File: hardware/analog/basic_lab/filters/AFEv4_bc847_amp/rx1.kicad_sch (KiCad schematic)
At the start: 7 parts, among them J7 Connector_Generic_Conn_01x02, J8 Connector_Generic_Conn_01x02

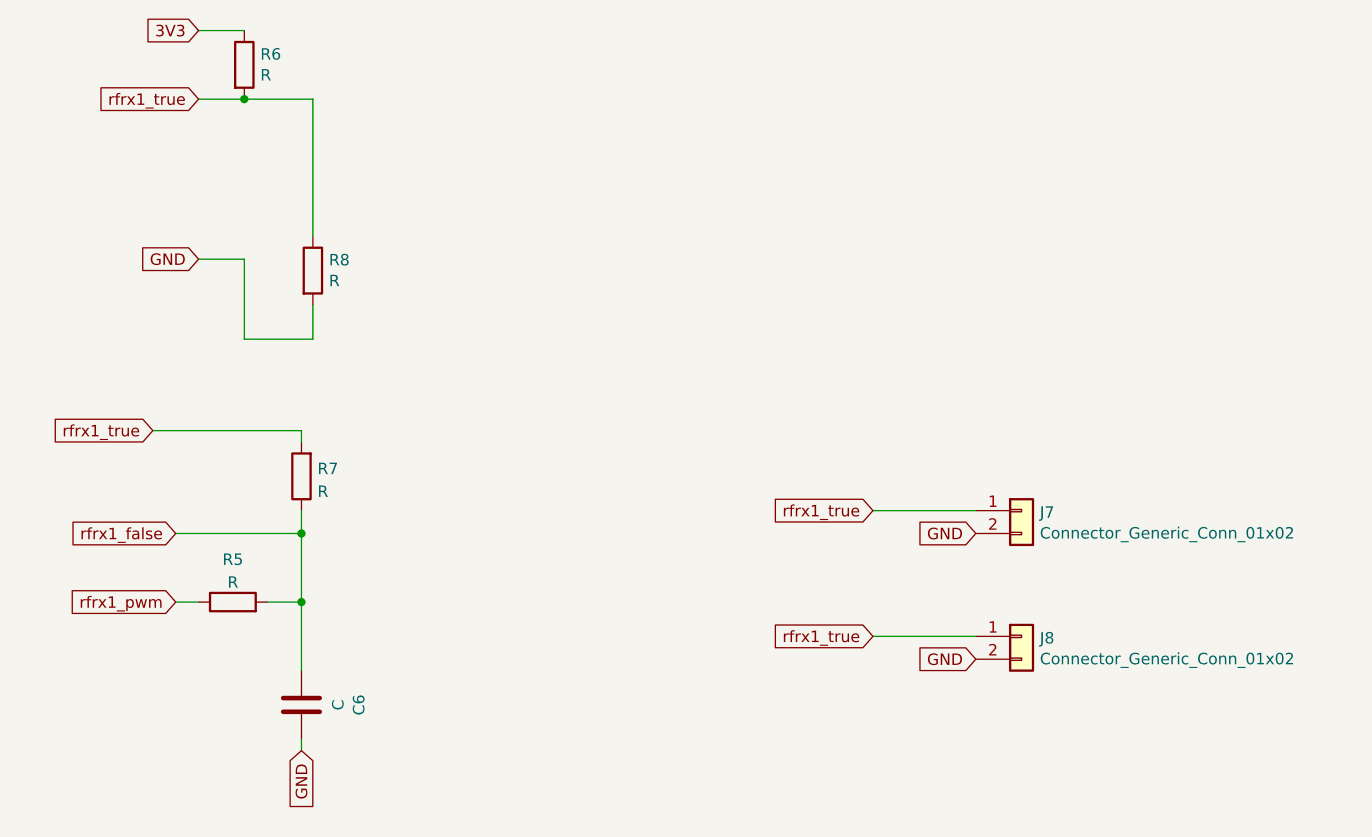
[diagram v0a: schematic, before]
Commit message: started PCB LC LPF
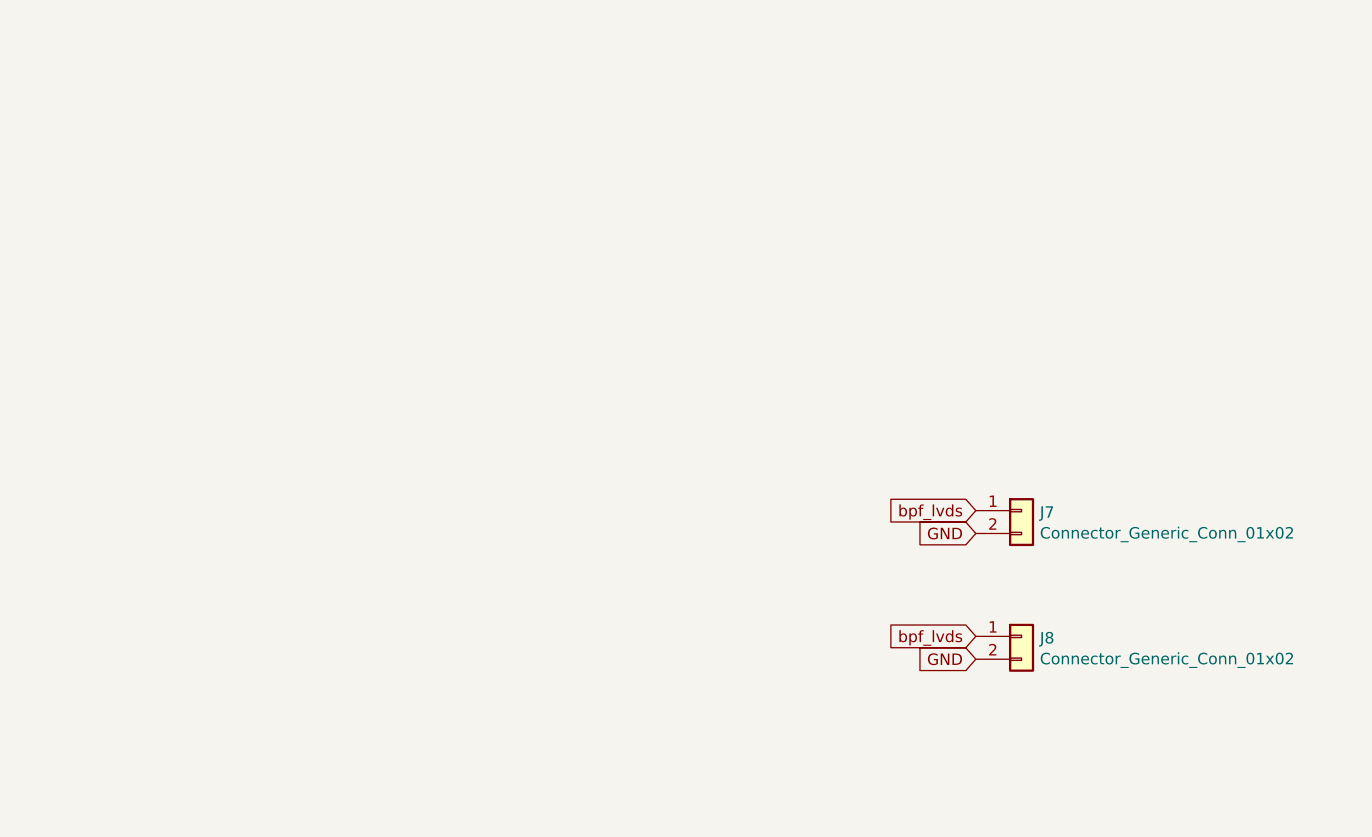
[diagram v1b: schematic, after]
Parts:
- removed C6: C, Capacitor_SMD:C_1206_3216Metric, symbol Device:C
- removed R5, R6, R7, R8: R, Resistor_SMD:R_1206_3216Metric, symbol Device:R
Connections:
- net rfrx1_true renamed bpf_lvds
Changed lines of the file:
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@@
 (kicad_sch (version 20211123) (generator eeschema)
   (paper "A4")
-  (junction (at 81.28 54.61) (diameter 0) (color 0 0 0 0)
-  )
-  (junction (at 87.63 110.49) (diameter 0) (color 0 0 0 0)
-  )
-  (junction (at 87.63 102.87) (diameter 0) (color 0 0 0 0)
-  )
-  (wire (pts (xy 81.28 72.39) (xy 81.28 81.28))
-    (stroke (width 0) (type default) (color 0 0 0 0))
-  )
-  (wire (pts (xy 81.28 54.61) (xy 88.9 54.61))
-    (stroke (width 0) (type default) (color 0 0 0 0))
-  )
-  (wire (pts (xy 151.13 114.3) (xy 162.56 114.3))
-    (stroke (width 0) (type default) (color 0 0 0 0))
-  )
-  (wire (pts (xy 87.63 110.49) (xy 87.63 118.11))
-    (stroke (width 0) (type default) (color 0 0 0 0))
-  )
-  (wire (pts (xy 76.2 72.39) (xy 81.28 72.39))
-    (stroke (width 0) (type default) (color 0 0 0 0))
-  )
-  (wire (pts (xy 87.63 125.73) (xy 87.63 127))
-    (stroke (width 0) (type default) (color 0 0 0 0))
-  )
-  (wire (pts (xy 71.12 91.44) (xy 87.63 91.44))
-    (stroke (width 0) (type default) (color 0 0 0 0))
-  )
-  (wire (pts (xy 81.28 81.28) (xy 88.9 81.28))
-    (stroke (width 0) (type default) (color 0 0 0 0))
-  )
-  (wire (pts (xy 76.2 46.99) (xy 81.28 46.99))
-    (stroke (width 0) (type default) (color 0 0 0 0))
-  )
-  (wire (pts (xy 87.63 100.33) (xy 87.63 102.87))
-    (stroke (width 0) (type default) (color 0 0 0 0))
-  )
-  (wire (pts (xy 151.13 100.33) (xy 162.56 100.33))
-    (stroke (width 0) (type default) (color 0 0 0 0))
-  )
-  (wire (pts (xy 87.63 102.87) (xy 87.63 110.49))
-    (stroke (width 0) (type default) (color 0 0 0 0))
-  )
-  (wire (pts (xy 73.66 110.49) (xy 76.2 110.49))
-    (stroke (width 0) (type default) (color 0 0 0 0))
-  )
-  (wire (pts (xy 73.66 102.87) (xy 87.63 102.87))
-    (stroke (width 0) (type default) (color 0 0 0 0))
-  )
-  (wire (pts (xy 88.9 81.28) (xy 88.9 77.47))
-    (stroke (width 0) (type default) (color 0 0 0 0))
-  )
-  (wire (pts (xy 87.63 91.44) (xy 87.63 92.71))
-    (stroke (width 0) (type default) (color 0 0 0 0))
-  )
-  (wire (pts (xy 88.9 54.61) (xy 88.9 69.85))
-    (stroke (width 0) (type default) (color 0 0 0 0))
-  )
-  (wire (pts (xy 76.2 54.61) (xy 81.28 54.61))
-    (stroke (width 0) (type default) (color 0 0 0 0))
-  )
-  (wire (pts (xy 83.82 110.49) (xy 87.63 110.49))
-    (stroke (width 0) (type default) (color 0 0 0 0))
-  )
   (global_label "GND" (shape input) (at 162.56 116.84 180) (fields_autoplaced)
     (effects (font (size 1.27 1.27)) (justify right))
     (property "Intersheet References" "${INTERSHEET_REFS}" (id 0) (at 1.27 -17.78 0)
       (effects (font (size 1.27 1.27)) hide)
-    )
-  )
-  (global_label "rfrx1_true" (shape input) (at 76.2 54.61 180) (fields_autoplaced)
-    (effects (font (size 1.27 1.27)) (justify right))
-    (property "Intersheet References" "${INTERSHEET_REFS}" (id 0) (at 64.6229 54.5306 0)
-      (effects (font (size 1.27 1.27)) (justify right) hide)
     )
   )
@@
     )
   )
-  (global_label "rfrx1_false" (shape input) (at 73.66 102.87 180) (fields_autoplaced)
+  (global_label "bpf_lvds" (shape input) (at 162.56 114.3 180) (fields_autoplaced)
     (effects (font (size 1.27 1.27)) (justify right))
-    (property "Intersheet References" "${INTERSHEET_REFS}" (id 0) (at 61.1758 102.7906 0)
-      (effects (font (size 1.27 1.27)) (justify right) hide)
-    )
-  )
-  (global_label "rfrx1_pwm" (shape input) (at 73.66 110.49 180) (fields_autoplaced)
-    (effects (font (size 1.27 1.27)) (justify right))
-    (property "Intersheet References" "${INTERSHEET_REFS}" (id 0) (at 61.6596 110.4106 0)
-      (effects (font (size 1.27 1.27)) (justify right) hide)
-    )
-  )
-  (global_label "GND" (shape input) (at 76.2 72.39 180) (fields_autoplaced)
-    (effects (font (size 1.27 1.27)) (justify right))
-    (property "Intersheet References" "${INTERSHEET_REFS}" (id 0) (at 1.27 -31.75 0)
+    (property "Intersheet References" "${INTERSHEET_REFS}" (id 0) (at 12.7 -17.78 0)
       (effects (font (size 1.27 1.27)) hide)
     )
   )
-  (global_label "rfrx1_true" (shape input) (at 71.12 91.44 180) (fields_autoplaced)
+  (global_label "bpf_lvds" (shape input) (at 162.56 100.33 180) (fields_autoplaced)
     (effects (font (size 1.27 1.27)) (justify right))
-    (property "Intersheet References" "${INTERSHEET_REFS}" (id 0) (at 59.5429 91.3606 0)
-      (effects (font (size 1.27 1.27)) (justify right) hide)
-    )
-  )
-  (global_label "3V3" (shape input) (at 76.2 46.99 180) (fields_autoplaced)
-    (effects (font (size 1.27 1.27)) (justify right))
-    (property "Intersheet References" "${INTERSHEET_REFS}" (id 0) (at 1.27 -31.75 0)
+    (property "Intersheet References" "${INTERSHEET_REFS}" (id 0) (at 12.7 -31.75 0)
       (effects (font (size 1.27 1.27)) hide)
     )
-  )
-  (global_label "GND" (shape input) (at 87.63 127 270) (fields_autoplaced)
-    (effects (font (size 1.27 1.27)) (justify right))
-    (property "Intersheet References" "${INTERSHEET_REFS}" (id 0) (at 222.25 43.18 0)
-      (effects (font (size 1.27 1.27)) hide)
-    )
-  )
-  (global_label "rfrx1_true" (shape input) (at 151.13 114.3 180) (fields_autoplaced)
-    (effects (font (size 1.27 1.27)) (justify right))
-    (property "Intersheet References" "${INTERSHEET_REFS}" (id 0) (at 139.5529 114.2206 0)
-      (effects (font (size 1.27 1.27)) (justify right) hide)
-    )
-  )
-  (global_label "rfrx1_true" (shape input) (at 151.13 100.33 180) (fields_autoplaced)
-    (effects (font (size 1.27 1.27)) (justify right))
-    (property "Intersheet References" "${INTERSHEET_REFS}" (id 0) (at 139.5529 100.2506 0)
-      (effects (font (size 1.27 1.27)) (justify right) hide)
-    )
-  )
-  (symbol (lib_id "Device:R") (at 87.63 96.52 180) (unit 1)
-    (in_bom yes) (on_board yes) (fields_autoplaced)
-    (property "Reference" "R7" (id 0) (at 89.408 95.6853 0)
-      (effects (font (size 1.27 1.27)) (justify right))
-    )
-    (property "Value" "R" (id 1) (at 89.408 98.2222 0)
-      (effects (font (size 1.27 1.27)) (justify right))
-    )
-    (property "Footprint" "Resistor_SMD:R_1206_3216Metric" (id 2) (at 89.408 96.52 90)
-      (effects (font (size 1.27 1.27)) hide)
-    )
-    (property "Datasheet" "~" (id 3) (at 87.63 96.52 0)
-      (effects (font (size 1.27 1.27)) hide)
-    )
-    (pin "1")
-    (pin "2")
-  )
-  (symbol (lib_id "Device:C") (at 87.63 121.92 180) (unit 1)
-    (in_bom yes) (on_board yes)
-    (property "Reference" "C6" (id 0) (at 94.0308 121.92 90))
-    (property "Value" "C" (id 1) (at 91.7194 121.92 90))
-    (property "Footprint" "Capacitor_SMD:C_1206_3216Metric" (id 2) (at 86.6648 118.11 0)
-      (effects (font (size 1.27 1.27)) hide)
-    )
-    (property "Datasheet" "~" (id 3) (at 87.63 121.92 0)
-      (effects (font (size 1.27 1.27)) hide)
-    )
-    (pin "1")
-    (pin "2")
-  )
-  (symbol (lib_id "Device:R") (at 88.9 73.66 0) (unit 1)
-    (in_bom yes) (on_board yes)
-    (property "Reference" "R8" (id 0) (at 90.678 72.4916 0)
-      (effects (font (size 1.27 1.27)) (justify left))
-    )
-    (property "Value" "R" (id 1) (at 90.678 74.803 0)
-      (effects (font (size 1.27 1.27)) (justify left))
-    )
-    (property "Footprint" "Resistor_SMD:R_1206_3216Metric" (id 2) (at 87.122 73.66 90)
-      (effects (font (size 1.27 1.27)) hide)
-    )
-    (property "Datasheet" "~" (id 3) (at 88.9 73.66 0)
-      (effects (font (size 1.27 1.27)) hide)
-    )
-    (pin "1")
-    (pin "2")
   )
   (symbol (lib_id "bgt:Connector_Generic_Conn_01x02") (at 167.64 114.3 0) (unit 1)
@@
     )
     (property "Datasheet" "" (id 3) (at 167.64 114.3 0)
-      (effects (font (size 1.27 1.27)) hide)
-    )
-    (pin "1")
-    (pin "2")
-  )
-  (symbol (lib_id "Device:R") (at 80.01 110.49 90) (unit 1)
-    (in_bom yes) (on_board yes) (fields_autoplaced)
-    (property "Reference" "R5" (id 0) (at 80.01 105.7742 90))
-    (property "Value" "R" (id 1) (at 80.01 108.3111 90))
-    (property "Footprint" "Resistor_SMD:R_1206_3216Metric" (id 2) (at 80.01 112.268 90)
-      (effects (font (size 1.27 1.27)) hide)
-    )
-    (property "Datasheet" "~" (id 3) (at 80.01 110.49 0)
       (effects (font (size 1.27 1.27)) hide)
     )
@@
       (effects (font (size 1.27 1.27)) hide)
     )
-    (pin "1")
-    (pin "2")
-  )
-  (symbol (lib_id "Device:R") (at 81.28 50.8 0) (unit 1)
-    (in_bom yes) (on_board yes)
-    (property "Reference" "R6" (id 0) (at 83.058 49.6316 0)
-      (effects (font (size 1.27 1.27)) (justify left))
-    )
-    (property "Value" "R" (id 1) (at 83.058 51.943 0)
-      (effects (font (size 1.27 1.27)) (justify left))
-    )
-    (property "Footprint" "Resistor_SMD:R_1206_3216Metric" (id 2) (at 79.502 50.8 90)
-      (effects (font (size 1.27 1.27)) hide)
-    )
-    (property "Datasheet" "~" (id 3) (at 81.28 50.8 0)
-      (effects (font (size 1.27 1.27)) hide)
-    )
